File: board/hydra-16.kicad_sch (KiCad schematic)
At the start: 35 parts, among them J1 Conn_01x32, J2 Conn_01x24, J27 RDY Pull_Up, J3 DSUB_9, U3 SST39SF0x0A, U4 W65C02S, U5 65C22, U6 65C51, U7 MAX232, U8 HM628512LP-5, U9 74F138

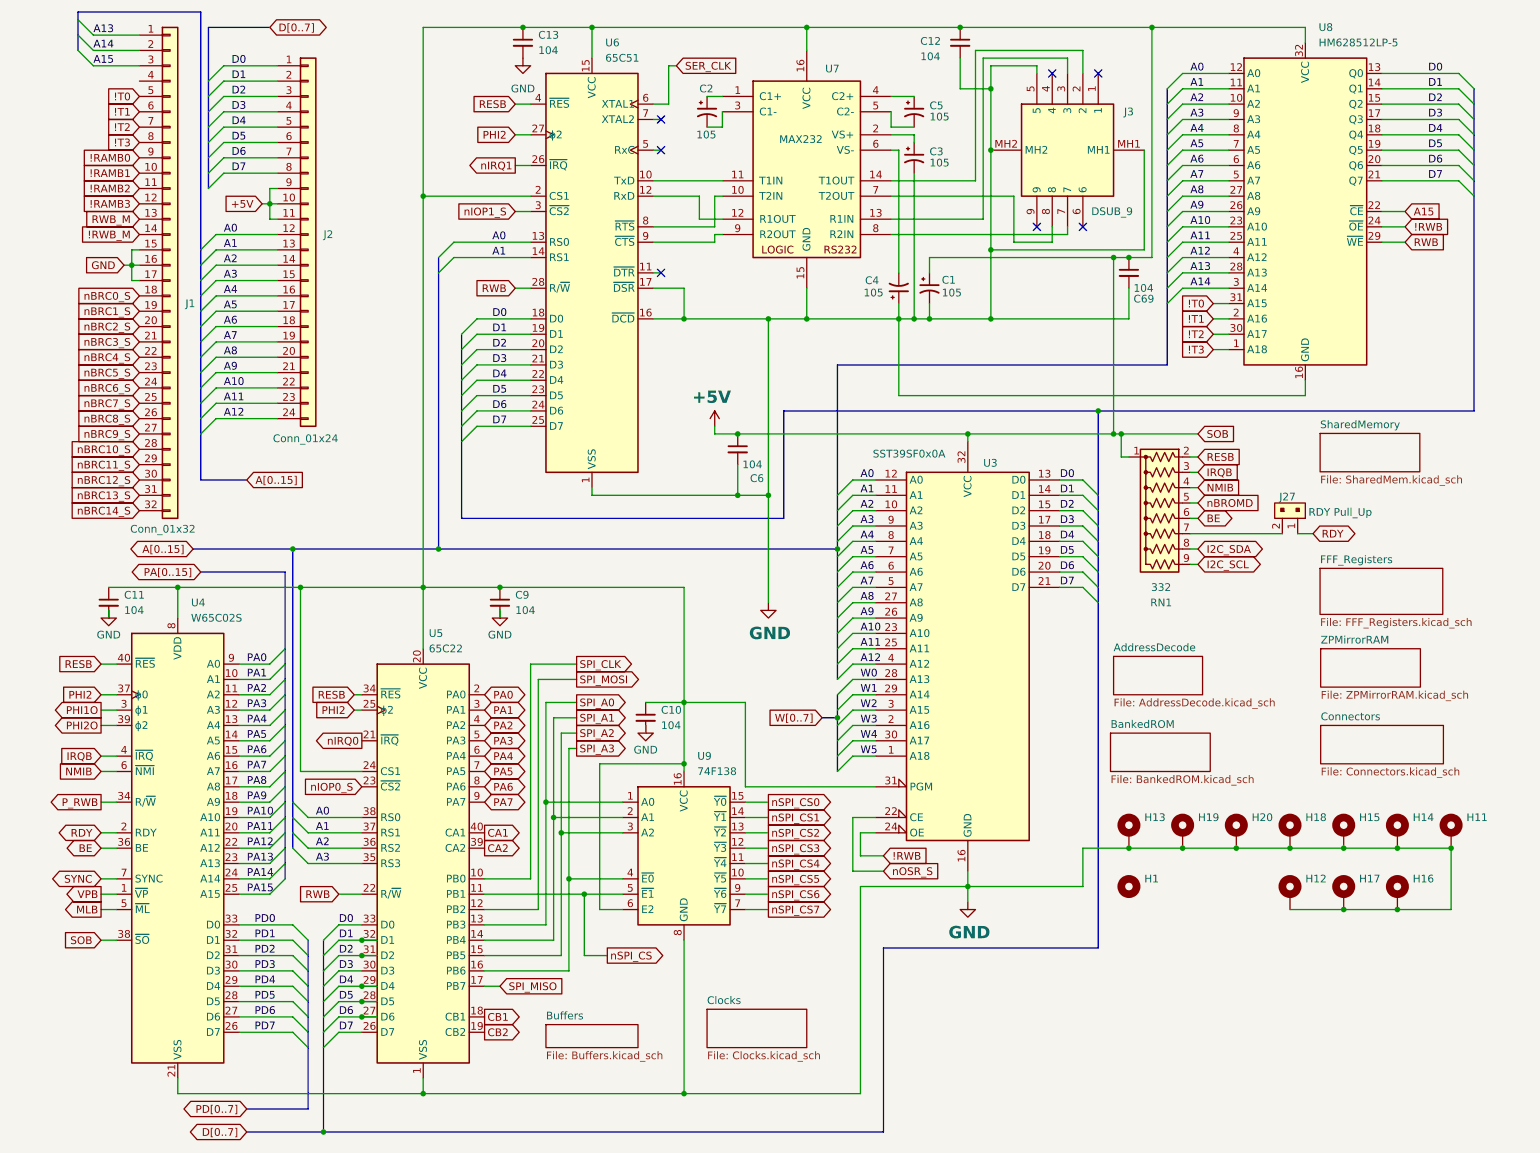
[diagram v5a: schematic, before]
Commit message: Version 1.7A: More rearrangement, partial wiring of PDB, addition of W register
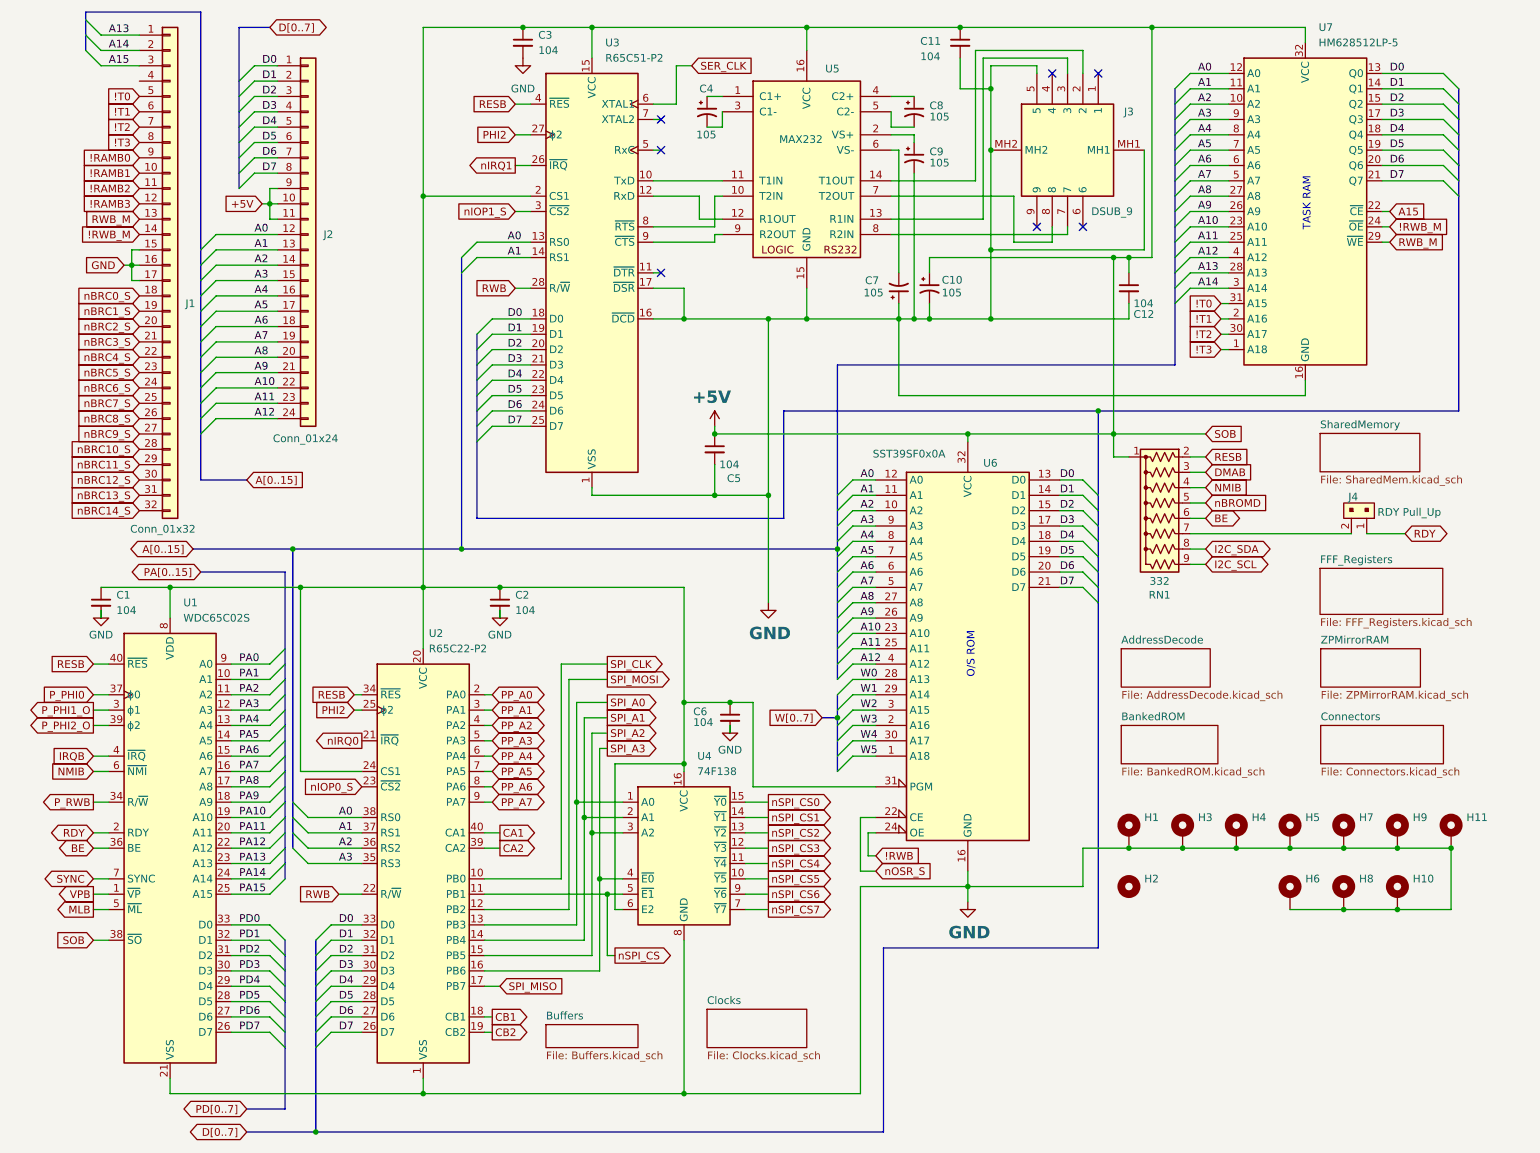
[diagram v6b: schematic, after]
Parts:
- U1: renamed from U4; value W65C02S -> WDC65C02S
- U2: renamed from U5; value 65C22 -> R65C22-P2
- U3: renamed from U6; value 65C51 -> R65C51-P2
- renumbered C11 to C1, C1 to C10, C12 to C11, C69 to C12, C9 to C2, C13 to C3, C2 to C4, C6 to C5, C10 to C6, C4 to C7, C5 to C8, C3 to C9, H13 to H1, H16 to H10, H1 to H2, H19 to H3, H20 to H4, H18 to H5, H12 to H6, H15 to H7, H17 to H8, H14 to H9, J27 to J4, U9 to U4, U7 to U5, U3 to U6, U8 to U7
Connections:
- net !RWB: no longer U7.24 (~{OE})
- net !RWB_M: now also U7.24 (~{OE})
- net IRQB: no longer RN1.3 (R2)
- net PA0: no longer U2.2 (PA0)
- net PA1: no longer U2.3 (PA1)
- net PA2: no longer U2.4 (PA2)
- net PA3: no longer U2.5 (PA3)
- net PA4: no longer U2.6 (PA4)
- net PA5: no longer U2.7 (PA5)
- net PA6: no longer U2.8 (PA6)
- net PA7: no longer U2.9 (PA7)
- net PHI2: no longer U1.37 (ϕ0)
- net RWB: no longer U7.29 (~{WE})
- net RWB_M: now also U7.29 (~{WE})
- net PHI1O renamed P_PHI1_O
- net PHI2O renamed P_PHI2_O
- new net DMAB: RN1.3 (R2)
- new net PP_A0: U2.2 (PA0)
- new net PP_A1: U2.3 (PA1)
- new net PP_A2: U2.4 (PA2)
- new net PP_A3: U2.5 (PA3)
- new net PP_A4: U2.6 (PA4)
- new net PP_A5: U2.7 (PA5)
- new net PP_A6: U2.8 (PA6)
- new net PP_A7: U2.9 (PA7)
- new net P_PHI0: U1.37 (ϕ0)
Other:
- note added: "O/S ROM"
- note added: "TASK RAM"
- moved on the sheet: C1, C12, C5, C6, J4, U1

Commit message: Version 1.7A: Partial wireup
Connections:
- net !RAMB0 renamed RAMB0_M
- net !RAMB1 renamed RAMB1_M
- net !RAMB2 renamed RAMB2_M
- net !RAMB3 renamed RAMB3_M
- net !T0 renamed T0_M
- net !T1 renamed T1_M
- net T1_M: now also U7.30 (A17)
- net !T2 renamed T2_M
- net T2_M: no longer U7.30 (A17)
- net !T3 renamed T3_M
